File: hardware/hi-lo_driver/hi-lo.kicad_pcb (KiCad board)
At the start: 2 copper layers, 66 x 97.2 mm, 119 parts, among them M200 CONN_1, M201 CONN_1, M202 CONN_1, P201 CONN_10X2, P202 CONN_3, P203 CONN_2, P204 CONN_1, P205 CONN_1, P208 CONN_6, P209 CONN_6, U201 LMV324IDR, U202 LMV324IDR, U203 LMV324IDR

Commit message: new version
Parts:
- removed C210, C220, C230, C240, C250, C260, C270, C280, C290, C300, C310, C320: 0.01uF, SM0805
- removed C211, C251, C291: 0.1uF, SM0805
- removed D210, D220, D230, D240, D250, D260, D270, D280, D290, D300, D310, D320: DOUBLE_SCHOTTKY, sot23
- removed G200: LOGO, LOGO
- removed G201: LOGO, LOGO_F
- removed LD200: LED, LED-1206
- removed M200, M201, M202, P204, P205: CONN_1, PIN_ARRAY_1
- removed P201: CONN_10X2, PIN_ARRAY_10X2_M
- removed P202: CONN_3, PIN_ARRAY_3X1
- removed P203: CONN_2, SIL-2
- removed P208, P209: CONN_6, PIN_ARRAY-6X1
- removed R200, R213, R223, R233, R243, R253, R263, R273, R283, R293, R303, R313, R323: 100, SM0805
- removed R210, R220, R230, R240, R250, R260, R270, R280, R290, R300, R310, R320: 2700, SM0805
- removed R211, R221, R231, R241, R251, R261, R271, R281, R291, R301, R311, R321: 500K, SM0805
- removed R212, R222, R232, R242, R252, R262, R272, R282, R292, R302, R312, R322: 10k, SM0805
- removed R214, R215, R224, R225, R234, R235, R244, R245, R254, R255, R264, R265, R274, R275, R284, R285, R294, R295, R304, R305, R314, R315, R324, R325: 1500, SM0805
- removed U201, U202, U203: LMV324IDR, so-14
- removed W211, W212: TEST, SIL-2
- added C1: 0.1uF, SM0805, F.Cu at (248.9, 194.3)
- added C2: 0.1uF, SM0805, F.Cu at (248.9, 201.9)
- added C3: 0.1uF, SM0805, F.Cu at (248.3, 186.7)
- added G1: LOGO, LOGO, F.Cu at (230.5, 181.0)
- added G2: LOGO, LOGO, F.Cu at (217.8, 181.0)
- added G3: LOGO, LOGO, F.Cu at (209.6, 181.0)
- added LD1: LED, SM1206, F.Cu at (261.6, 187.3)
- added LD2: LED, SM1206, F.Cu at (261.6, 191.1)
- added LD3: LED, SM1206, F.Cu at (261.6, 194.9)
- added LD4: LED, SM1206, F.Cu at (261.6, 198.8)
- added LD5: LED, SM1206, F.Cu at (261.6, 202.6)
- added LD6: LED, SM1206, F.Cu at (261.6, 206.4)
- added M1: CONN_1, 1pin, F.Cu at (240.7, 167.6)
- added M2: CONN_1, 1pin, F.Cu at (240.7, 174.0)
- added M3: CONN_1, 1pin, F.Cu at (240.7, 180.3)
- added P1: CONN_3X2, pin_array_3x2, F.Cu at (238.1, 196.8)
- added P2: CONN_2, SIL-2, F.Cu at (244.5, 196.8)
- added P3: CONN_6, SIL-6, F.Cu at (269.2, 196.8)
- added R1: 100, SM0805, F.Cu at (256.5, 188.0)
- added R10: 2700, SM0805, F.Cu at (252.7, 201.9)
- added R11: 2700, SM0805, F.Cu at (252.7, 207.0)
- added R12: 100, SM0805, F.Cu at (256.5, 205.7)
- added R2: 2700, SM0805, F.Cu at (252.1, 186.7)
- added R3: 2700, SM0805, F.Cu at (252.1, 191.8)
- added R4: 100, SM0805, F.Cu at (256.5, 190.5)
- added R5: 100, SM0805, F.Cu at (256.5, 195.6)
- added R6: 2700, SM0805, F.Cu at (252.7, 194.3)
- added R7: 2700, SM0805, F.Cu at (252.1, 199.4)
- added R8: 100, SM0805, F.Cu at (256.5, 198.1)
- added R9: 100, SM0805, F.Cu at (256.5, 203.2)
- added U1: TC4427AVOA, msoic-8, F.Cu at (250.8, 189.2)
- added U2: TC4427AVOA, msoic-8, F.Cu at (250.8, 196.8)
- added U3: TC4427AVOA, msoic-8, F.Cu at (250.8, 204.5)
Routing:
- net /5V: track 176.8 -> 0.00 mm
- net /OUT2: track 23.6 -> 0.00 mm
- net GND: track 21.0 -> 0.00 mm
- net /INP1: track 16.8 -> 0.00 mm
- net /OUT1: track 16.3 -> 0.00 mm
- net /INP2: track 14.2 -> 0.00 mm
- net N-0000083: track 13.9 -> 0.00 mm
- net N-0000078: track 8.87 -> 0.00 mm
- net N-000008: track 6.53 -> 0.00 mm
- net N-000005: track 6.53 -> 0.00 mm
- net N-0000015: track 4.51 -> 0.00 mm
- net N-0000012: track 4.51 -> 0.00 mm
- net N-0000039: track 2.54 -> 0.00 mm
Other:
- board text removed: "INP10"
- board text removed: "INP11"
- board text removed: "INP12"
- board text removed: "PA5"
- board text removed: "rusEfi.com 12ch r 0.01"

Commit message: fitted into F
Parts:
- moved C3 72.7 mm to (184.2, 152.4)
- moved P1 71.0 mm to (179.1, 157.5)
- moved LD6 65.3 mm to (212.1, 163.8)
- moved P3 63.5 mm to (218.4, 158.8)
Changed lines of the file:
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@@
     (links 48)
     (no_connects 48)
-    (area 120.639999 93.334999 186.700001 190.510001)
+    (area 28.778999 12.121499 264.744201 255.053501)
     (thickness 1.6)
-    (drawings 27)
+    (drawings 33)
     (tracks 0)
     (zones 0)
@@
   )
   (module SM1206 (layer F.Cu)
-    (at 261.62 206.375)
+    (at 212.09 163.83)
     (attr smd)
     (fp_text reference LD6 (at 0 0 90) (layer F.SilkS)
@@
   )
   (module SM0805 (layer F.Cu)
-    (at 248.285 186.69)
+    (at 184.15 152.4)
     (attr smd)
     (fp_text reference C3 (at 0 -0.3175 90) (layer F.SilkS)
@@
   )
   (module SIL-6 (layer F.Cu)
-    (at 269.24 196.85 270)
+    (at 218.44 158.75 270)
     (descr "Connecteur 6 pins")
     (tags "CONN DEV")
@@
   )
   (module pin_array_3x2 (layer F.Cu)
-    (at 238.125 196.85 270)
+    (at 179.07 157.48 270)
     (descr "Double rangee de contacts 2 x 4 pins")
     (tags CONN)
@@
     )
   )
+  (gr_line (start 213.36 165.1) (end 213.36 166.37) (angle 90) (layer Eco2.User) (width 0.1))
+  (gr_line (start 219.71 166.37) (end 213.36 166.37) (angle 90) (layer Eco2.User) (width 0.1))
+  (gr_line (start 170.18 165.1) (end 170.18 151.13) (angle 90) (layer Eco2.User) (width 0.1))
+  (gr_line (start 213.36 165.1) (end 170.18 165.1) (angle 90) (layer Eco2.User) (width 0.1))
+  (gr_line (start 219.71 151.13) (end 219.71 166.37) (angle 90) (layer Eco2.User) (width 0.1))
+  (gr_line (start 170.18 151.13) (end 219.71 151.13) (angle 90) (layer Eco2.User) (width 0.1))
   (gr_text IAT (at 121.666 107.061) (layer B.SilkS)
     (effects (font (size 0.508 0.508) (thickness 0.127)) (justify mirror))

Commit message: new version
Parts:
- removed G2, G3: LOGO, LOGO
- removed G202: LOGO, LOGO_F
- removed M1, M2, M3: CONN_1, 1pin
- G1: moved to B.Cu
- moved LD3 77.2 mm to (195.6, 154.9), turned to 90 degrees
- moved LD4 75.9 mm to (195.6, 161.3), turned to 270 degrees
- moved R6 75.8 mm to (188.0, 154.9)
- moved R5 75.5 mm to (191.8, 156.8)
- moved R8 75.5 mm to (191.8, 159.4)
- moved U2 75.5 mm to (186.1, 158.1)
- moved R7 74.6 mm to (188.0, 161.3)
- moved P2 68.5 mm to (191.8, 153.0), turned to 180 degrees
- moved R12 65.3 mm to (207.0, 163.2)
- moved C2 65.3 mm to (199.4, 159.4)
- moved R10 65.3 mm to (203.2, 159.4)
- moved R9 65.3 mm to (207.0, 160.7)
- moved LD5 65.3 mm to (212.1, 160.0)
- moved U3 65.3 mm to (201.3, 161.9)
- moved R11 64.8 mm to (203.8, 164.5)
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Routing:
- net /VP: track 0.00 -> 58.2 mm, vias 0 -> 3
- net N-000005: track 0.00 -> 30.1 mm
- net /HL4: track 0.00 -> 26.8 mm
- net /HL3: track 0.00 -> 26.3 mm
- net N-000004: track 0.00 -> 24.7 mm
- net N-000003: track 0.00 -> 23.9 mm
- net N-000002: track 0.00 -> 20.8 mm
- net GND: track 0.00 -> 19.1 mm, vias 0 -> 11
- net /HL6: track 0.00 -> 12.1 mm
- net /HL1: track 0.00 -> 11.3 mm
- net /HL5: track 0.00 -> 11.3 mm
- net /HL2: track 0.00 -> 11.2 mm
- net N-0000012: track 0.00 -> 7.35 mm
- net N-0000011: track 0.00 -> 7.35 mm
- net N-0000014: track 0.00 -> 7.03 mm
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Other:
- board size 66 x 97.2 mm -> 49.5 x 15.5 mm
- board text added: "HI-LO1"
- board text added: "HI-LO2"
- board text added: "HI-LO3"
- board text added: "HI-LO4"
- board text added: "HI-LO5"
- board text added: "HI-LO6"
- board text added: "VP"
- board text added: "for RUSEFI.com"
- board text added: "https://code.google.com/p/daecu/ R.01"
- board text removed: "5v"
- board text removed: "CLT"
- board text removed: "IAT"
- board text removed: "PC0"
- board text removed: "TPS"

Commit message: mounting hole
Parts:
- added M601: CONN_1, PIN_ARRAY_1, F.Cu at (181.9, 163.4)
- G1: footprint LOGO -> LOGO_F
- moved G1 38.5 mm to (210.3, 173.0)
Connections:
- net N-000002 renamed /H_IN6
- net N-000003 renamed /H_IN5
- net N-000004 renamed /H_IN1
- net N-000005 renamed /H_IN3
- net N-000009 renamed /H_IN2
- P1 pad 4: N-000006 (its old number) -> /H_IN4
- U2 pad 4: N-000006 (its old number) -> /H_IN4
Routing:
- net N-000006 (its old number): track 4.08 -> 0.00 mm
- net /H_IN4: track 0.00 -> 4.08 mm
- net /H_IN6: track 20.8 -> 22.3 mm
- net /H_IN5: track 23.9 -> 25.0 mm
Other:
- board size 49.5 x 15.5 mm -> 43.2 x 15.5 mm

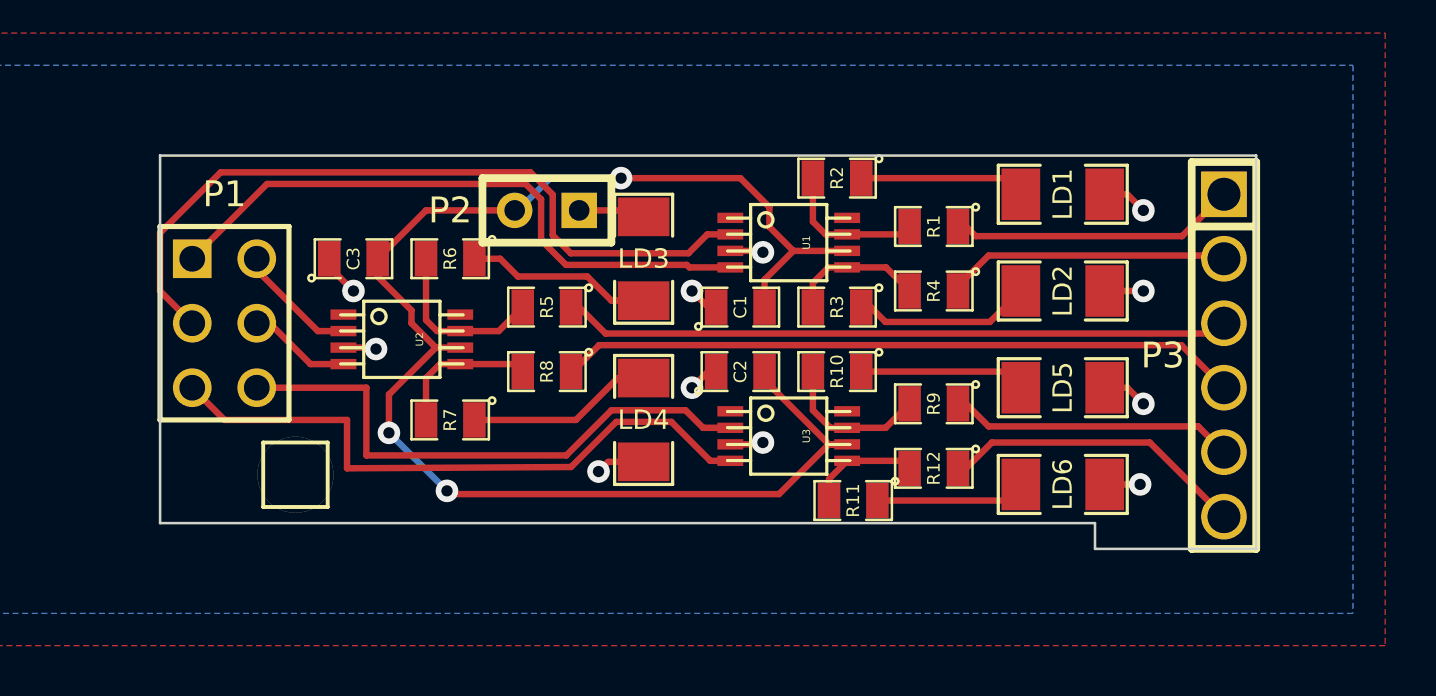
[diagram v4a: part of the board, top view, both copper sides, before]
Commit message: 
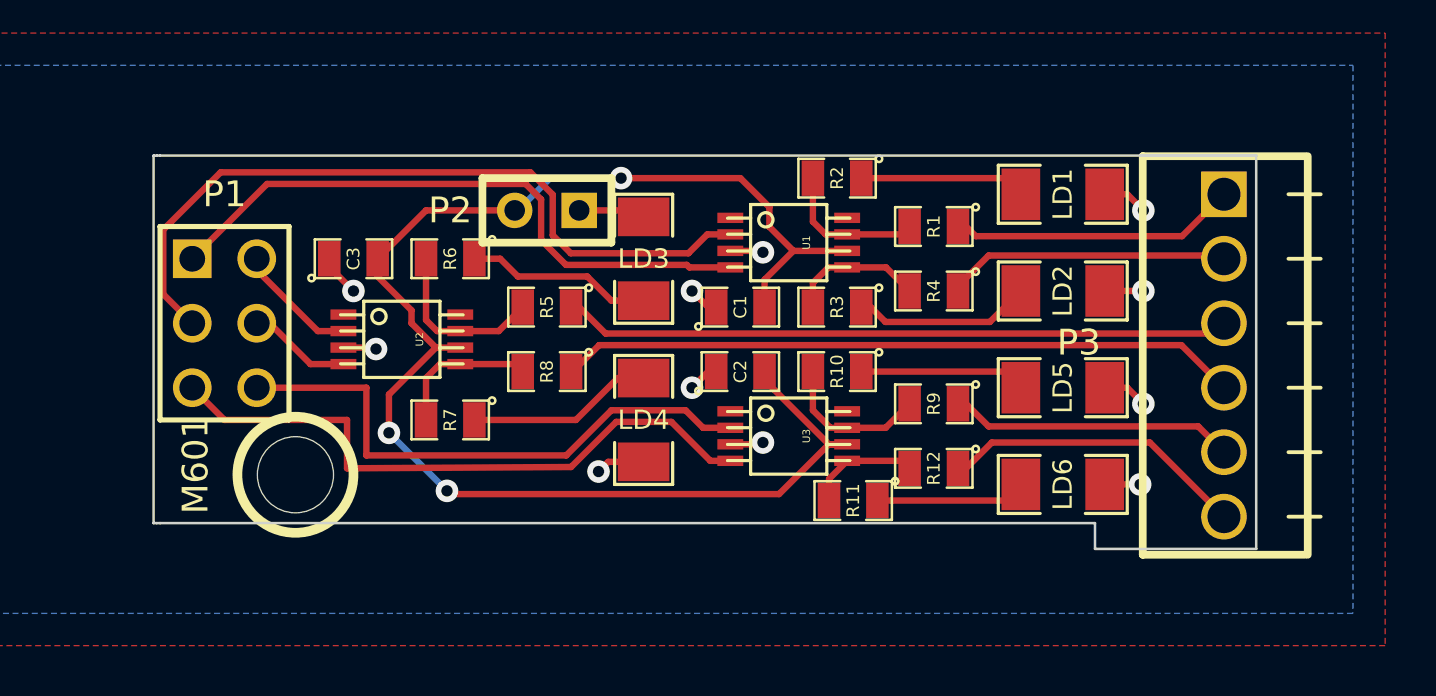
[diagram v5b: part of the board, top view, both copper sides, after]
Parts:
- M601: footprint PIN_ARRAY_1 -> 1pin
- P3: footprint SIL-6 -> OSTVN06A150
- moved G1 29.6 mm to (184.3, 158.9)
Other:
- board size 43.2 x 15.5 mm -> 43.4 x 15.5 mm
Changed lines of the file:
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@@
     (area 28.778999 12.121499 224.790001 255.053501)
     (thickness 1.6)
-    (drawings 68)
+    (drawings 72)
     (tracks 173)
     (zones 0)
@@
     (pad_to_mask_clearance 0)
     (aux_axis_origin 0 0)
-    (visible_elements 7FFFFBBF)
+    (visible_elements 7FFFFB3F)
     (pcbplotparams
       (layerselection 317751297)
@@
     )
   )
-  (module SIL-6 (layer F.Cu)
-    (at 218.44 158.75 270)
-    (descr "Connecteur 6 pins")
-    (tags "CONN DEV")
-    (fp_text reference P3 (at 0 2.413 360) (layer F.SilkS)
-      (effects (font (size 1.016 1.016) (thickness 0.2032)))
-    )
-    (fp_text value CONN_6 (at 0 -2.54 270) (layer F.SilkS) hide
-      (effects (font (size 1.524 1.016) (thickness 0.3048)))
-    )
-    (fp_line (start -7.62 1.27) (end -7.62 -1.27) (layer F.SilkS) (width 0.3048))
-    (fp_line (start -7.62 -1.27) (end 7.62 -1.27) (layer F.SilkS) (width 0.3048))
-    (fp_line (start 7.62 -1.27) (end 7.62 1.27) (layer F.SilkS) (width 0.3048))
-    (fp_line (start 7.62 1.27) (end -7.62 1.27) (layer F.SilkS) (width 0.3048))
-    (fp_line (start -5.08 1.27) (end -5.08 -1.27) (layer F.SilkS) (width 0.3048))
-    (pad 1 thru_hole rect (at -6.35 0 270) (size 1.8 1.8) (drill 1.3)
-      (layers *.Cu *.Mask F.SilkS)
-      (net 1 /HL1)
-    )
-    (pad 2 thru_hole circle (at -3.81 0 270) (size 1.8 1.8) (drill 1.3)
-      (layers *.Cu *.Mask F.SilkS)
-      (net 2 /HL2)
-    )
-    (pad 3 thru_hole circle (at -1.27 0 270) (size 1.8 1.8) (drill 1.3)
-      (layers *.Cu *.Mask F.SilkS)
-      (net 3 /HL3)
-    )
-    (pad 4 thru_hole circle (at 1.27 0 270) (size 1.8 1.8) (drill 1.3)
-      (layers *.Cu *.Mask F.SilkS)
-      (net 4 /HL4)
-    )
-    (pad 5 thru_hole circle (at 3.81 0 270) (size 1.8 1.8) (drill 1.3)
-      (layers *.Cu *.Mask F.SilkS)
-      (net 5 /HL5)
-    )
-    (pad 6 thru_hole circle (at 6.35 0 270) (size 1.8 1.8) (drill 1.3)
-      (layers *.Cu *.Mask F.SilkS)
-      (net 6 /HL6)
-    )
-  )
   (module SIL-2 (layer F.Cu)
     (at 191.77 153.035 180)
@@
     )
   )
+  (module OSTVN06A150 (layer F.Cu)
+    (at 218.44 158.75 270)
+    (fp_text reference P3 (at -0.508 5.715 360) (layer F.SilkS)
+      (effects (font (size 1.016 1.016) (thickness 0.2032)))
+    )
+    (fp_text value CONN_6 (at 0 5.08 270) (layer F.SilkS) hide
+      (effects (font (size 1.524 1.016) (thickness 0.254)))
+    )
+    (fp_line (start 6.35 -2.54) (end 6.35 -3.81) (layer F.SilkS) (width 0.15))
+    (fp_line (start 3.81 -2.54) (end 3.81 -3.81) (layer F.SilkS) (width 0.15))
+    (fp_line (start 1.27 -2.54) (end 1.27 -3.81) (layer F.SilkS) (width 0.15))
+    (fp_line (start -1.27 -2.54) (end -1.27 -3.81) (layer F.SilkS) (width 0.15))
+    (fp_line (start -3.81 -2.54) (end -3.81 -3.81) (layer F.SilkS) (width 0.15))
+    (fp_line (start -6.35 -2.54) (end -6.35 -3.81) (layer F.SilkS) (width 0.15))
+    (fp_line (start -7.85 3.2) (end -7.85 -3.2) (layer F.SilkS) (width 0.3048))
+    (fp_line (start -7.85 -3.3) (end 7.85 -3.3) (layer F.SilkS) (width 0.3048))
+    (fp_line (start 7.85 -3.2) (end 7.85 3.2) (layer F.SilkS) (width 0.3048))
+    (fp_line (start 7.85 3.2) (end -7.85 3.2) (layer F.SilkS) (width 0.3048))
+    (pad 1 thru_hole rect (at -6.35 0 270) (size 1.8 1.8) (drill 1.3)
+      (layers *.Cu *.Mask F.SilkS)
+      (net 1 /HL1)
+    )
+    (pad 2 thru_hole circle (at -3.81 0 270) (size 1.8 1.8) (drill 1.3)
+      (layers *.Cu *.Mask F.SilkS)
+      (net 2 /HL2)
+    )
+    (pad 3 thru_hole circle (at -1.27 0 270) (size 1.8 1.8) (drill 1.3)
+      (layers *.Cu *.Mask F.SilkS)
+      (net 3 /HL3)
+    )
+    (pad 4 thru_hole circle (at 1.27 0 270) (size 1.8 1.8) (drill 1.3)
+      (layers *.Cu *.Mask F.SilkS)
+      (net 4 /HL4)
+    )
+    (pad 5 thru_hole circle (at 3.81 0 270) (size 1.8 1.8) (drill 1.3)
+      (layers *.Cu *.Mask F.SilkS)
+      (net 5 /HL5)
+    )
+    (pad 6 thru_hole circle (at 6.35 0 270) (size 1.8 1.8) (drill 1.3)
+      (layers *.Cu *.Mask F.SilkS)
+      (net 6 /HL6)
+    )
+  )
+  (module 1pin (layer F.Cu)
+    (at 181.864 163.449)
+    (descr "module 1 pin (ou trou mecanique de percage)")
+    (tags DEV)
+    (fp_text reference M601 (at -3.937 -0.381 90) (layer F.SilkS)
+      (effects (font (size 1.016 1.016) (thickness 0.254)))
+    )
+    (fp_text value CONN_1 (at 0 2.794) (layer F.SilkS) hide
+      (effects (font (size 1.016 1.016) (thickness 0.254)))
+    )
+    (fp_circle (center 0 0) (end 0 -2.286) (layer F.SilkS) (width 0.381))
+    (pad "" np_thru_hole circle (at 0 0) (size 3 3) (drill 3)
+      (layers *.Cu *.Mask F.SilkS)
+    )
+  )
   (module LOGO_F (layer B.Cu)
-    (at 210.312 172.974)
+    (at 184.277 158.877)
     (fp_text reference G1 (at 0 -4.14782) (layer B.SilkS) hide
       (effects (font (size 1.524 1.524) (thickness 0.3048)) (justify mirror))
@@
       (xy 3.3401 -0.50546) (xy 3.34264 -0.09398) (xy 3.34518 -0.04318) (xy 3.34518 -0.04318)) (layer B.SilkS) (width 0.00254))
   )
-  (module PIN_ARRAY_1 (layer F.Cu)
-    (at 181.864 163.449)
-    (descr "1 pin")
-    (tags "CONN DEV")
-    (fp_text reference M601 (at 0 -1.905) (layer F.SilkS) hide
-      (effects (font (size 0.762 0.762) (thickness 0.1524)))
-    )
-    (fp_text value CONN_1 (at 0 -1.905) (layer F.SilkS) hide
-      (effects (font (size 0.762 0.762) (thickness 0.1524)))
-    )
-    (fp_line (start 1.27 1.27) (end -1.27 1.27) (layer F.SilkS) (width 0.1524))
-    (fp_line (start -1.27 -1.27) (end 1.27 -1.27) (layer F.SilkS) (width 0.1524))
-    (fp_line (start -1.27 1.27) (end -1.27 -1.27) (layer F.SilkS) (width 0.1524))
-    (fp_line (start 1.27 -1.27) (end 1.27 1.27) (layer F.SilkS) (width 0.1524))
-    (pad 1 thru_hole circle (at 0 0) (size 3 3) (drill 3)
-      (layers *.Cu *.Mask F.SilkS)
-    )
-    (model pin_array\pin_1.wrl
-      (at (xyz 0 0 0))
-      (scale (xyz 1 1 1))
-      (rotate (xyz 0 0 0))
-    )
-  )
+  (gr_line (start 176.403 165.354) (end 176.276 165.354) (angle 90) (layer Edge.Cuts) (width 0.1))
+  (gr_line (start 176.276 150.876) (end 176.403 150.876) (angle 90) (layer Edge.Cuts) (width 0.1))
+  (gr_line (start 176.53 165.354) (end 176.403 165.354) (angle 90) (layer Edge.Cuts) (width 0.1))
+  (gr_line (start 176.53 150.876) (end 176.403 150.876) (angle 90) (layer Edge.Cuts) (width 0.1))
   (gr_line (start 219.71 150.876) (end 219.71 166.37) (angle 90) (layer Edge.Cuts) (width 0.1))
   (gr_line (start 176.53 150.876) (end 219.71 150.876) (angle 90) (layer Edge.Cuts) (width 0.1))
-  (gr_line (start 176.53 165.354) (end 176.53 150.876) (angle 90) (layer Edge.Cuts) (width 0.1))
+  (gr_line (start 176.276 165.354) (end 176.276 150.876) (angle 90) (layer Edge.Cuts) (width 0.1))
   (gr_line (start 213.36 165.354) (end 176.53 165.354) (angle 90) (layer Edge.Cuts) (width 0.1))
   (gr_line (start 213.36 165.354) (end 213.36 166.37) (angle 90) (layer Edge.Cuts) (width 0.1))
@@
   (gr_line (start 120.65 93.345) (end 186.69 93.345) (angle 90) (layer Eco2.User) (width 0.02))
   (gr_line (start 186.69 190.5) (end 186.69 93.345) (angle 90) (layer Eco2.User) (width 0.02))
-  (gr_text "for RUSEFI.com" (at 189.865 160.02) (layer B.SilkS)
+  (gr_text "for RUSEFI.com" (at 206.375 160.401) (layer B.SilkS)
     (effects (font (size 1.016 1.016) (thickness 0.2032)) (justify mirror))
   )
@@
   (segment (start 182.74538 157.78988) (end 180.34 155.3845) (width 0.254) (layer F.Cu) (net 8))
   (segment (start 198.99376 153.97988) (end 198.08952 153.97988) (width 0.254) (layer F.Cu) (net 9))
-  (segment (start 176.53 156.21) (end 177.8 157.48) (width 0.254) (layer F.Cu) (net 9))
-  (segment (start 176.53 153.924) (end 176.53 156.21) (width 0.254) (layer F.Cu) (net 9))
-  (segment (start 178.917602 151.536398) (end 176.53 153.924) (width 0.254) (layer F.Cu) (net 9))
+  (segment (start 176.657 156.337) (end 177.8 157.48) (width 0.254) (layer F.Cu) (net 9))
+  (segment (start 176.657 153.797) (end 176.657 156.337) (width 0.254) (layer F.Cu) (net 9))
+  (segment (start 178.917602 151.536398) (end 176.657 153.797) (width 0.254) (layer F.Cu) (net 9))
   (segment (start 191.12118 151.536398) (end 178.917602 151.536398) (width 0.254) (layer F.Cu) (net 9))
   (segment (start 191.998602 152.41382) (end 191.12118 151.536398) (width 0.254) (layer F.Cu) (net 9))

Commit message: fixing 3D
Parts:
- G1: footprint LOGO_F -> LOGO
